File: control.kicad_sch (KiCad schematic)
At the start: 69 parts, among them J5 MCU disable, J6 TC2030, J7 LED, J8 USB-C, U4 ADS7142, U5 RPMH3.3-0.5, U6 ESP32-C3, U7 ADS7142, U8 ECMF02-2AMX6

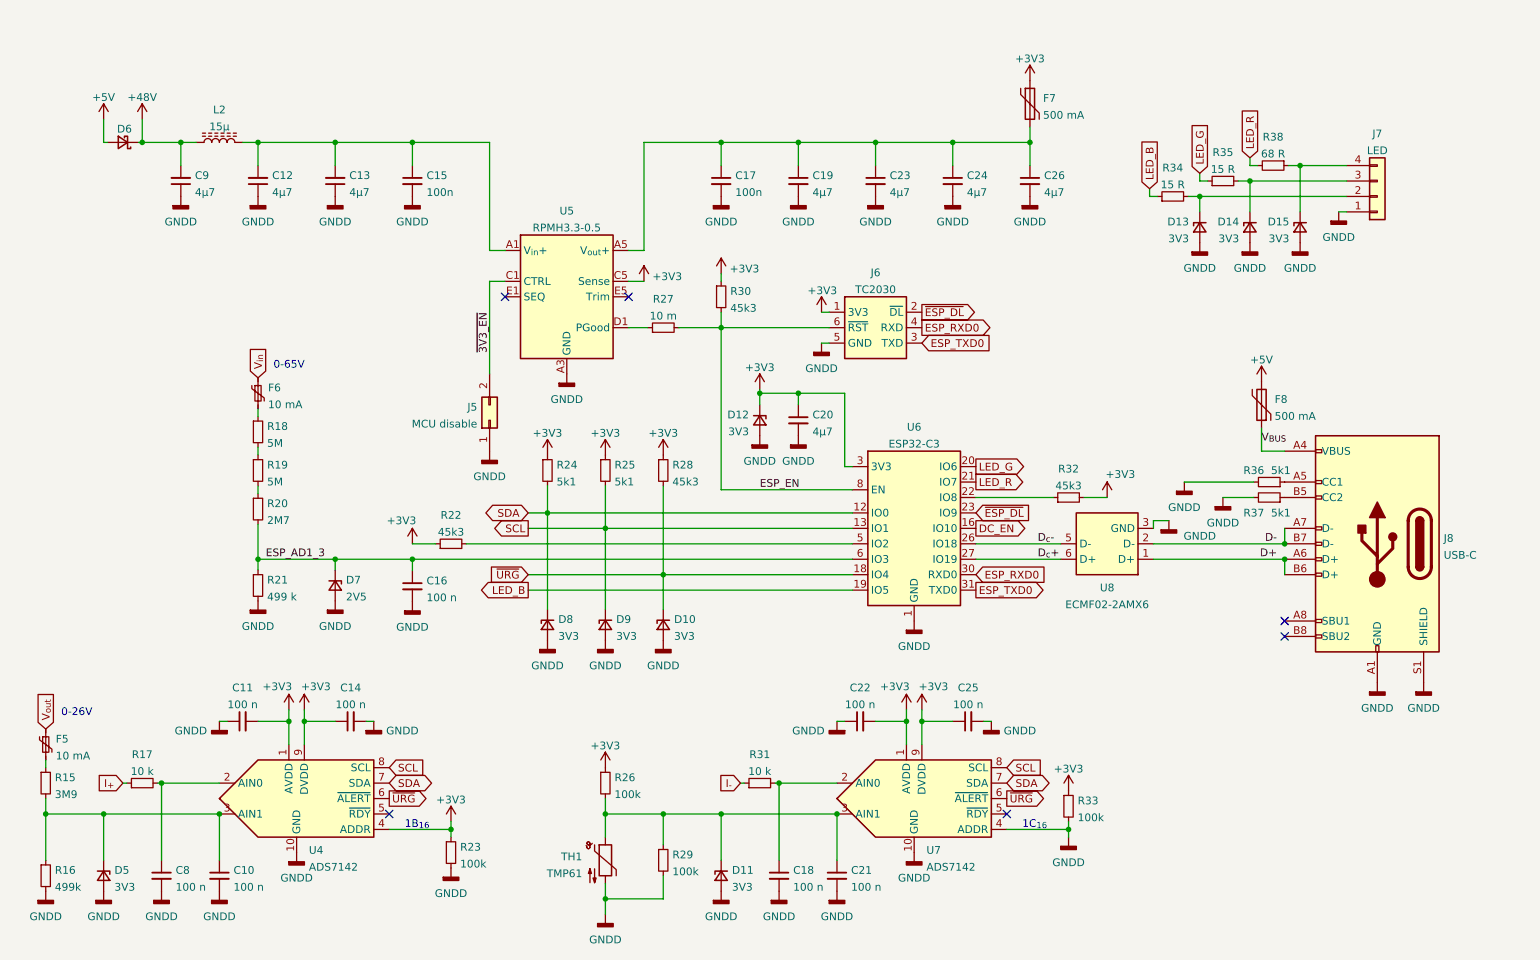
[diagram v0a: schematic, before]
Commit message: Add 100 nF bypass capacitor to ESP32 power input
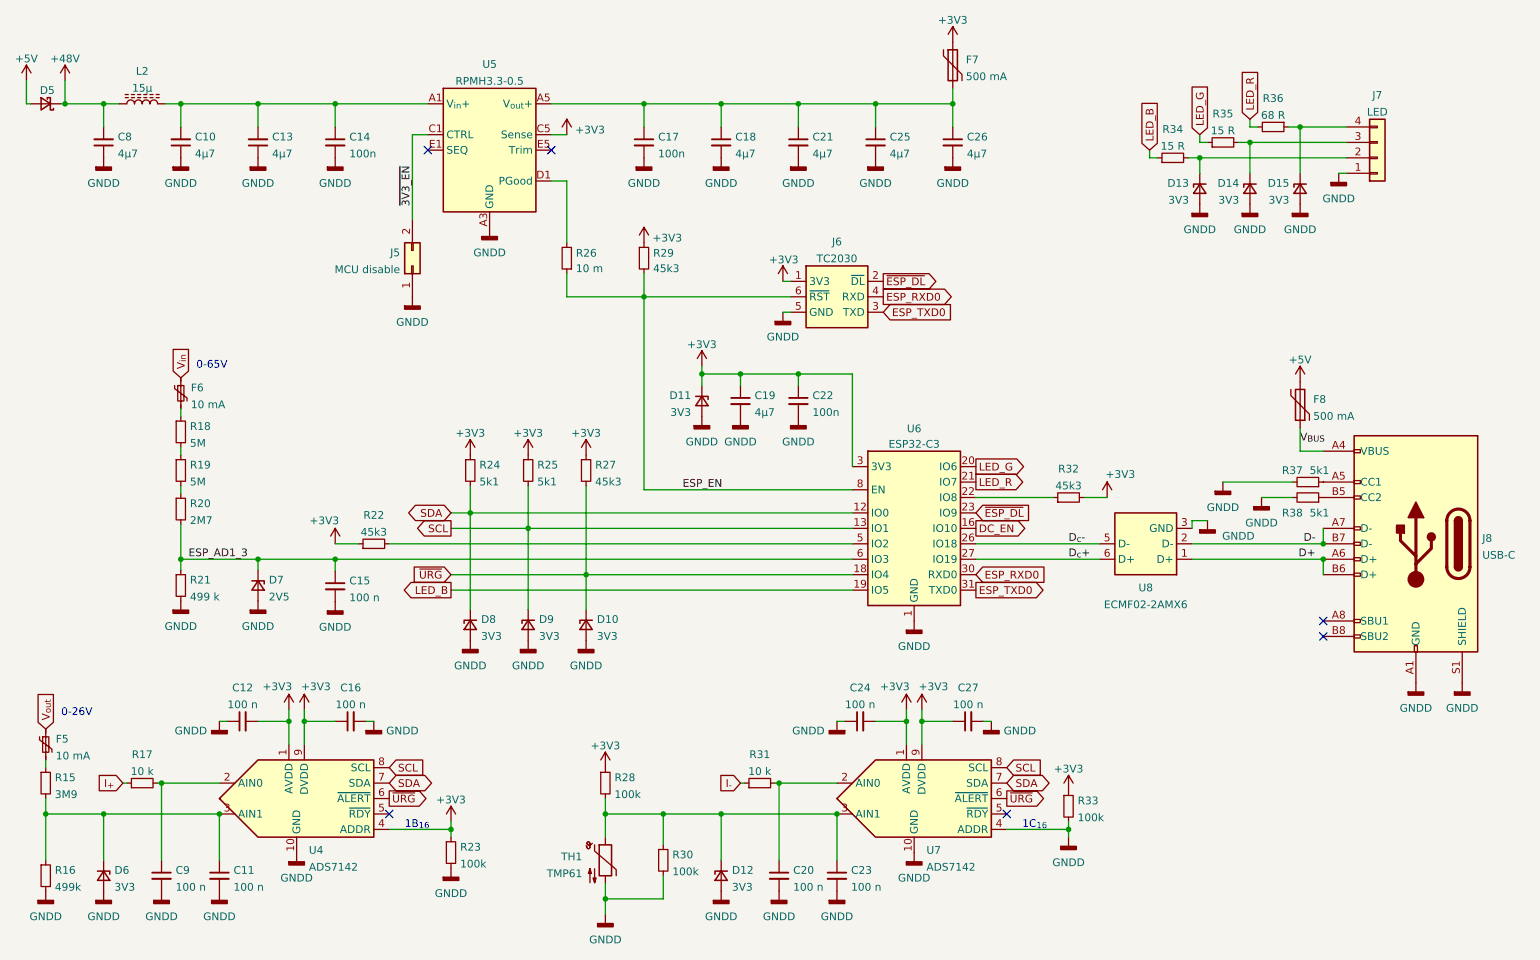
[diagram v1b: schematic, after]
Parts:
- added C22: 100n, Capacitor_SMD:C_0402_1005Metric, symbol Device:C_Small
- renumbered C12 to C10, C10 to C11, C11 to C12, C15 to C14, C16 to C15, C14 to C16, C19 to C18, C20 to C19, C18 to C20, C23 to C21, C21 to C23, C22 to C24, C24 to C25, C25 to C27, C9 to C8, C8 to C9, D12 to D11, D11 to D12, D6 to D5, D5 to D6, R27 to R26, R28 to R27, R26 to R28, R30 to R29, R29 to R30, R38 to R36, R36 to R37, R37 to R38
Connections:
- net +3V3: now also C22.1
- net ESP_EN: now also R26.1; no longer R26.2
- net GND: now also C22.2
- net at U5.D1 (PGood): now also R26.2; no longer R26.1
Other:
- moved on the sheet: C10, C13, C14, C15, C17, C18, C19, C21, C25, C26, C8, D10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

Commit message: Increase power input filter capacitance
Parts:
- C12, C24: value 100 n -> 220 n; Manufacturer Taiyo Yuden -> Murata; Part Number JMK105B7104KV-F -> GCM155R71C224KE02D
- C19, C26: value 4µ7 -> 10µ; Part Number GRM21BR71A475KE51L -> GRM21BR71A106KA73K
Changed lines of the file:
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@@
+    (pin "2")
+  )
+  (symbol (lib_id "Device:C_Small") (at 67.31 133.35 90) (unit 1)
+    (in_bom yes) (on_board yes) (fields_autoplaced)
+    (property "Reference" "C12" (id 0) (at 67.3163 128.0881 90))
+    (property "Value" "220 n" (id 1) (at 67.3163 130.625 90))
+    (property "Footprint" "Capacitor_SMD:C_0402_1005Metric" (id 2) (at 67.31 133.35 0)
+      (effects (font (size 1.27 1.27)) hide)
+    )
+    (property "Datasheet" "~" (id 3) (at 67.31 133.35 0)
+      (effects (font (size 1.27 1.27)) hide)
+    )
+    (property "Manufacturer" "Murata" (id 4) (at 67.31 133.35 0)
+      (effects (font (size 1.27 1.27)) hide)
+    )
+    (property "Part Number" "GCM155R71C224KE02D" (id 5) (at 67.31 133.35 0)
+      (effects (font (size 1.27 1.27)) hide)
+    )
+    (pin "1")
     (pin "2")
   )
@@
     )
     (pin "1")
+  )
+  (symbol (lib_id "Device:C_Small") (at 184.15 38.1 0) (unit 1)
+    (in_bom yes) (on_board yes) (fields_autoplaced)
+    (property "Reference" "C26" (id 0) (at 186.4741 37.2716 0)
+      (effects (font (size 1.27 1.27)) (justify left))
+    )
+    (property "Value" "10µ" (id 1) (at 186.4741 39.8085 0)
+      (effects (font (size 1.27 1.27)) (justify left))
+    )
+    (property "Footprint" "Capacitor_SMD:C_0805_2012Metric" (id 2) (at 184.15 38.1 0)
+      (effects (font (size 1.27 1.27)) hide)
+    )
+    (property "Datasheet" "~" (id 3) (at 184.15 38.1 0)
+      (effects (font (size 1.27 1.27)) hide)
+    )
+    (property "Manufacturer" "Murata" (id 4) (at 184.15 38.1 0)
+      (effects (font (size 1.27 1.27)) hide)
+    )
+    (property "Part Number" "GRM21BR71A106KA73K" (id 5) (at 184.15 38.1 0)
+      (effects (font (size 1.27 1.27)) hide)
+    )
+    (pin "1")
+    (pin "2")
   )
   (symbol (lib_id "power:GNDD") (at 146.05 161.29 0) (unit 1)
@@
   (symbol (lib_id "Device:C_Small") (at 168.91 133.35 90) (unit 1)
     (in_bom yes) (on_board yes) (fields_autoplaced)
-    (property "Reference" "C24" (id 0) (at 168.9163 127.8214 90))
-    (property "Value" "100 n" (id 1) (at 168.9163 130.5965 90))
+    (property "Reference" "C24" (id 0) (at 168.9163 128.0881 90))
+    (property "Value" "220 n" (id 1) (at 168.9163 130.625 90))
     (property "Footprint" "Capacitor_SMD:C_0402_1005Metric" (id 2) (at 168.91 133.35 0)
       (effects (font (size 1.27 1.27)) hide)
@@
       (effects (font (size 1.27 1.27)) hide)
     )
-    (property "Manufacturer" "Taiyo Yuden" (id 4) (at 168.91 133.35 0)
-      (effects (font (size 1.27 1.27)) hide)
-    )
-    (property "Part Number" " JMK105B7104KV-F" (id 5) (at 168.91 133.35 0)
-      (effects (font (size 1.27 1.27)) hide)
-    )
-    (pin "1")
-    (pin "2")
-  )
-  (symbol (lib_id "Device:C_Small") (at 67.31 133.35 90) (unit 1)
-    (in_bom yes) (on_board yes) (fields_autoplaced)
-    (property "Reference" "C12" (id 0) (at 67.3163 127.8214 90))
-    (property "Value" "100 n" (id 1) (at 67.3163 130.5965 90))
-    (property "Footprint" "Capacitor_SMD:C_0402_1005Metric" (id 2) (at 67.31 133.35 0)
-      (effects (font (size 1.27 1.27)) hide)
-    )
-    (property "Datasheet" "~" (id 3) (at 67.31 133.35 0)
-      (effects (font (size 1.27 1.27)) hide)
-    )
-    (property "Manufacturer" "Taiyo Yuden" (id 4) (at 67.31 133.35 0)
-      (effects (font (size 1.27 1.27)) hide)
-    )
-    (property "Part Number" " JMK105B7104KV-F" (id 5) (at 67.31 133.35 0)
+    (property "Manufacturer" "Murata" (id 4) (at 168.91 133.35 0)
+      (effects (font (size 1.27 1.27)) hide)
+    )
+    (property "Part Number" "GCM155R71C224KE02D" (id 5) (at 168.91 133.35 0)
       (effects (font (size 1.27 1.27)) hide)
     )
@@
   (symbol (lib_id "Device:C_Small") (at 149.225 80.645 0) (unit 1)
     (in_bom yes) (on_board yes) (fields_autoplaced)
-    (property "Reference" "C19" (id 0) (at 151.5491 79.7428 0)
-      (effects (font (size 1.27 1.27)) (justify left))
-    )
-    (property "Value" "4µ7" (id 1) (at 151.5491 82.5179 0)
+    (property "Reference" "C19" (id 0) (at 151.5491 79.8166 0)
+      (effects (font (size 1.27 1.27)) (justify left))
+    )
+    (property "Value" "10µ" (id 1) (at 151.5491 82.3535 0)
       (effects (font (size 1.27 1.27)) (justify left))
     )
@@
       (effects (font (size 1.27 1.27)) hide)
     )
-    (property "Part Number" "GRM21BR71A475KE51L" (id 5) (at 149.225 80.645 0)
+    (property "Part Number" "GRM21BR71A106KA73K" (id 5) (at 149.225 80.645 0)
       (effects (font (size 1.27 1.27)) hide)
     )
@@
       (effects (font (size 1.27 1.27)) hide)
     )
-    (pin "1")
-    (pin "2")
-  )
-  (symbol (lib_id "Device:C_Small") (at 184.15 38.1 0) (unit 1)
-    (in_bom yes) (on_board yes) (fields_autoplaced)
-    (property "Reference" "C26" (id 0) (at 186.4741 37.1978 0)
-      (effects (font (size 1.27 1.27)) (justify left))
-    )
-    (property "Value" "4µ7" (id 1) (at 186.4741 39.9729 0)
-      (effects (font (size 1.27 1.27)) (justify left))
-    )
-    (property "Footprint" "Capacitor_SMD:C_0805_2012Metric" (id 2) (at 184.15 38.1 0)
-      (effects (font (size 1.27 1.27)) hide)
-    )
-    (property "Datasheet" "~" (id 3) (at 184.15 38.1 0)
-      (effects (font (size 1.27 1.27)) hide)
-    )
-    (property "Manufacturer" "Murata" (id 4) (at 184.15 38.1 0)
-      (effects (font (size 1.27 1.27)) hide)
-    )
-    (property "Part Number" "GRM21BR71A475KE51L" (id 5) (at 184.15 38.1 0)
-      (effects (font (size 1.27 1.27)) hide)
-    )
